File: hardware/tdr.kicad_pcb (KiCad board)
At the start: 4 copper layers, 101 x 47 mm, 240 parts, among them J201 Conn_02x01, J202 Conn_Coaxial, J203 Conn_Coaxial, J204 Conn_Coaxial, J205 Conn_Coaxial, J207 Conn_Coaxial, J208 Conn_Coaxial, J209 Conn_Coaxial, J210 Barrel_Jack_Switch, J801 Conn_02x06_Counter_Clockwise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

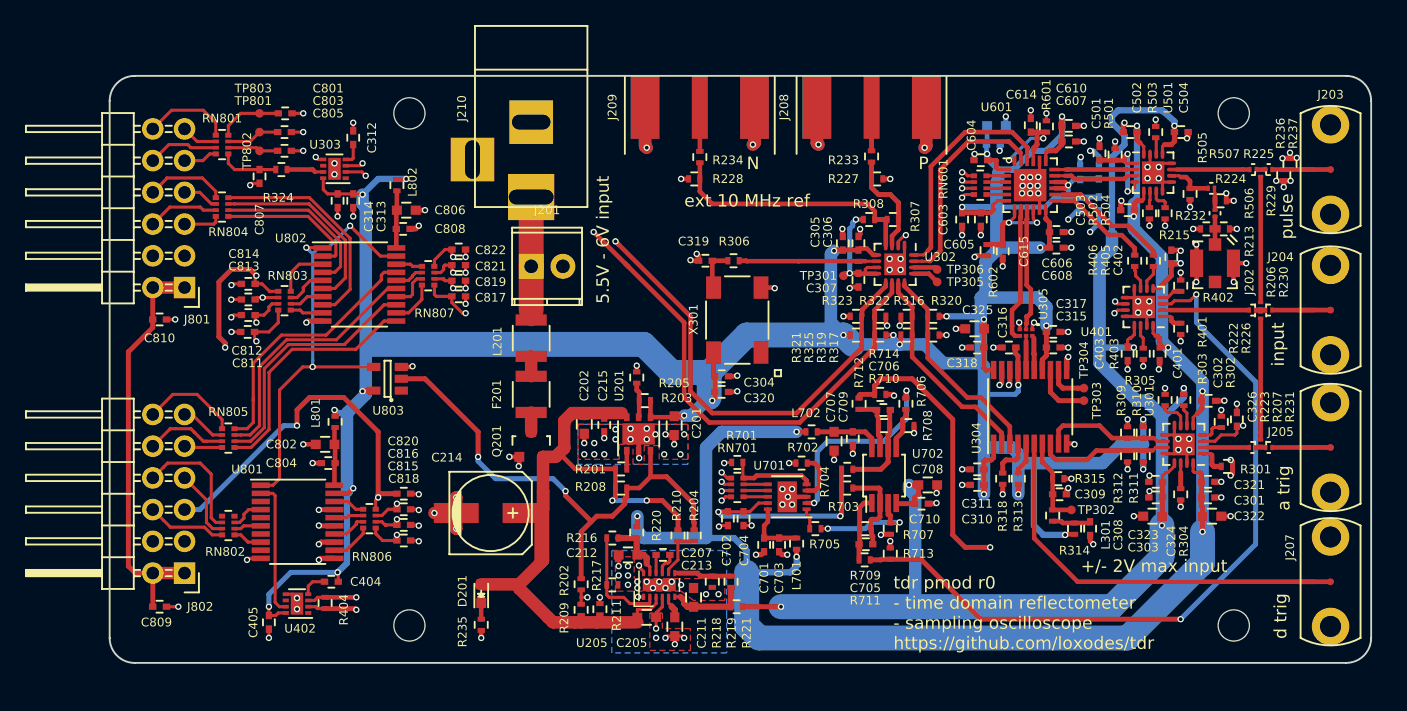
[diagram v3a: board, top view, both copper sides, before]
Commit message: cleanup of tdr layout
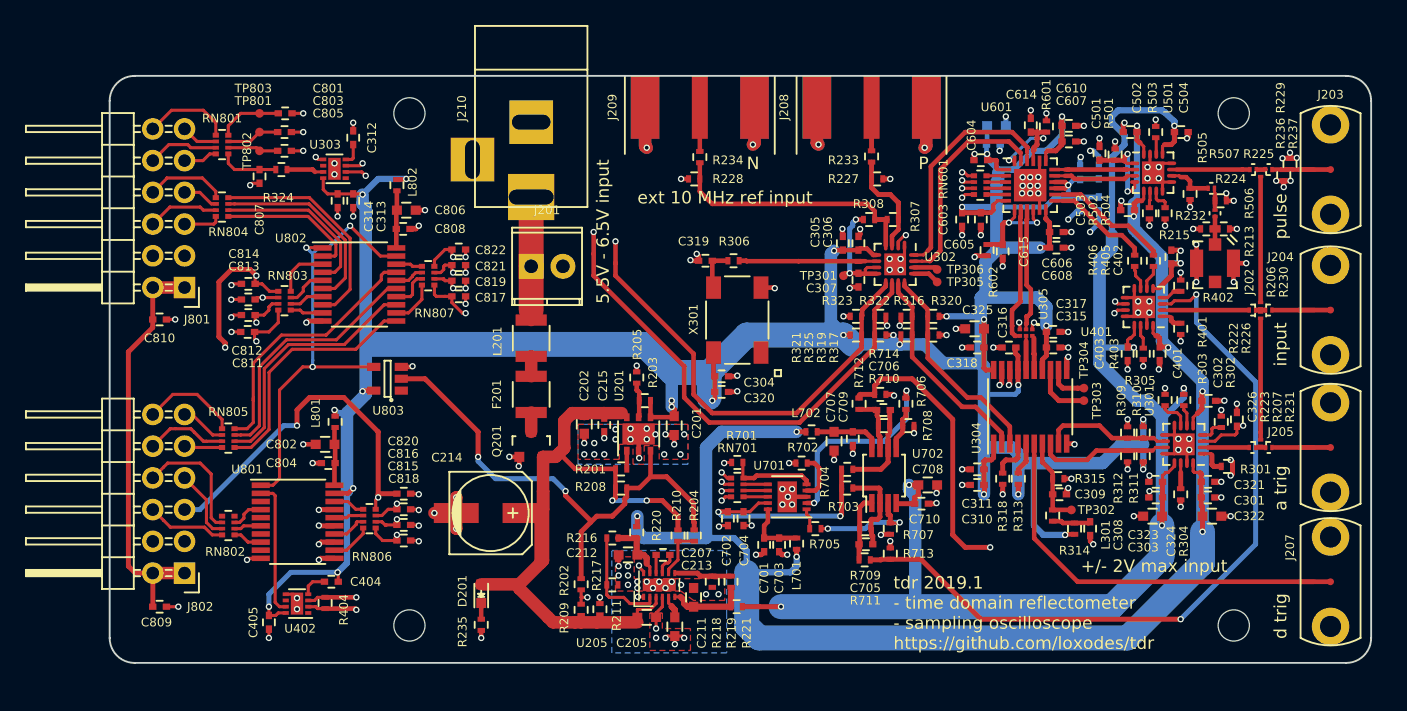
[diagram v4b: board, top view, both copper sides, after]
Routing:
- net +3V3: track 270.6 -> 271.2 mm, vias 27 -> 28
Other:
- rule pad_to_mask_clearance: 0.025 -> 0
- rule solder_mask_min_width: 0.25 -> 0.15
- board text added: "5.5V - 6.5V input"
- board text added: "ext 10 MHz ref input"
- board text added: "tdr 2019.1 - time domain reflectometer - sampling oscilloscope https://github.com/loxodes/tdr"
- board text removed: "5.5V - 6V input"
- board text removed: "ext 10 MHz ref"
- board text removed: "tdr pmod r0 - time domain reflectometer - sampling oscilloscope https://github.com/loxodes/tdr"
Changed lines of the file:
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@@
     (thickness 1.6)
     (drawings 18)
-    (tracks 2160)
+    (tracks 2161)
     (zones 0)
     (modules 240)
@@
   (layers
     (0 F.Cu signal)
-    (1 In1.Cu signal hide)
+    (1 In1.Cu signal)
     (2 In2.Cu signal)
     (31 B.Cu signal)
@@
   )
   (setup
-    (last_trace_width 0.5)
+    (last_trace_width 0.25)
     (user_trace_width 0.37)
     (user_trace_width 0.4)
@@
     (pad_size 1.524 1.524)
     (pad_drill 0.762)
-    (pad_to_mask_clearance 0.025)
-    (solder_mask_min_width 0.25)
+    (pad_to_mask_clearance 0)
+    (solder_mask_min_width 0.15)
     (aux_axis_origin 0 0)
     (visible_elements FFFDFF7F)
@@
     (tags "resistor 0402")
     (attr smd)
-    (fp_text reference R203 (at 2.55 -0.2) (layer F.SilkS)
+    (fp_text reference R203 (at 0.65 -2.25 90) (layer F.SilkS)
       (effects (font (size 0.7 0.7) (thickness 0.15)))
     )
@@
     (tags "resistor 0402")
     (attr smd)
-    (fp_text reference R205 (at 0.45 -3) (layer F.SilkS)
+    (fp_text reference R205 (at -2.65 -0.05 90) (layer F.SilkS)
       (effects (font (size 0.7 0.7) (thickness 0.15)))
     )
@@
     (tags "resistor 0201")
     (attr smd)
-    (fp_text reference R229 (at -0.2 -2.5 270) (layer F.SilkS)
+    (fp_text reference R229 (at -0.95 5.75 270) (layer F.SilkS)
       (effects (font (size 0.7 0.7) (thickness 0.15)))
     )
@@
     (effects (font (size 1 1) (thickness 0.25)) (justify left))
   )
-  (gr_text "ext 10 MHz ref" (at 135 69) (layer F.SilkS)
+  (gr_text "ext 10 MHz ref input" (at 131.25 68.75) (layer F.SilkS)
     (effects (font (size 1 1) (thickness 0.25)) (justify left))
   )
-  (gr_text "5.5V - 6V input\n" (at 128.5 77.25 90) (layer F.SilkS)
+  (gr_text "5.5V - 6.5V input\n" (at 128.5 77.25 90) (layer F.SilkS)
     (effects (font (size 1 1) (thickness 0.25)) (justify left))
   )
-  (gr_text "tdr pmod r0\n- time domain reflectometer\n- sampling oscilloscope\nhttps://github.com/loxodes/tdr" (at 151.75 102) (layer F.SilkS)
+  (gr_text "tdr 2019.1\n- time domain reflectometer\n- sampling oscilloscope\nhttps://github.com/loxodes/tdr" (at 151.75 102) (layer F.SilkS)
     (effects (font (size 1 1) (thickness 0.25)) (justify left))
   )
@@
     (effects (font (size 1 1) (thickness 0.25)))
   )
-  (gr_text "a trig" (at 183 92 90) (layer F.SilkS)
+  (gr_text "a trig" (at 182.75 92 90) (layer F.SilkS)
     (effects (font (size 1 1) (thickness 0.25)))
   )
-  (gr_text input (at 182.55 80.5 90) (layer F.SilkS)
+  (gr_text input (at 182.75 80.5 90) (layer F.SilkS)
     (effects (font (size 1 1) (thickness 0.25)))
   )
-  (gr_text pulse (at 183.25 70.25 90) (layer F.SilkS)
+  (gr_text pulse (at 182.75 70.25 90) (layer F.SilkS)
     (effects (font (size 1 1) (thickness 0.25)))
   )
@@
   (segment (start 134.122357 86.327643) (end 134.2 86.25) (width 0.37) (layer F.Cu) (net 2))
   (segment (start 132.302946 86.327643) (end 134.122357 86.327643) (width 0.37) (layer F.Cu) (net 2))
-  (via (at 135 86.2) (size 0.51) (drill 0.3) (layers F.Cu B.Cu) (net 2))
-  (segment (start 134.2 86.25) (end 134.95 86.25) (width 0.37) (layer F.Cu) (net 2))
-  (segment (start 134.95 86.25) (end 135 86.2) (width 0.37) (layer F.Cu) (net 2))
   (segment (start 160.075 66.5) (end 160 66.425) (width 0.25) (layer F.Cu) (net 2))
   (segment (start 160.75 66.5) (end 160.075 66.5) (width 0.25) (layer F.Cu) (net 2))
@@
   (segment (start 137 82.75) (end 140 79.75) (width 2) (layer B.Cu) (net 2))
   (segment (start 140 79.75) (end 147.75 79.75) (width 2) (layer B.Cu) (net 2))
-  (segment (start 135.55 86.2) (end 137 84.75) (width 1) (layer B.Cu) (net 2))
-  (segment (start 135 86.2) (end 135.55 86.2) (width 1) (layer B.Cu) (net 2))
   (segment (start 109.25 68.5) (end 109.25 69.25) (width 1) (layer B.Cu) (net 2))
   (segment (start 109.25 69.25) (end 109.5 69.5) (width 1) (layer B.Cu) (net 2))
@@
   (segment (start 165.25 63.75) (end 164 65) (width 0.5) (layer B.Cu) (net 2))
   (segment (start 165.25 62.25) (end 165.25 63.75) (width 0.5) (layer B.Cu) (net 2))
+  (via (at 134 85.5) (size 0.51) (drill 0.3) (layers F.Cu B.Cu) (net 2))
+  (segment (start 134 85.5) (end 134 82.75) (width 1) (layer B.Cu) (net 2))
+  (via (at 134 85) (size 0.51) (drill 0.3) (layers F.Cu B.Cu) (net 2))
+  (segment (start 134 85.5) (end 134 85) (width 0.4) (layer F.Cu) (net 2))
+  (segment (start 134 85.5) (end 134.2 85.7) (width 0.4) (layer F.Cu) (net 2))
+  (segment (start 134.2 86.25) (end 134.2 85.7) (width 0.4) (layer F.Cu) (net 2))
   (segment (start 123.4 94) (end 123.7 93.7) (width 1) (layer F.Cu) (net 3))
   (segment (start 122.25082 94) (end 123.4 94) (width 1) (layer F.Cu) (net 3))
@@
   (segment (start 149.2 78.25) (end 149.2 79.75) (width 0.37) (layer F.Cu) (net 58))
   (segment (start 149.2 79.75) (end 149.2 80.42) (width 0.37) (layer F.Cu) (net 58))
-  (segment (start 149.2 79.75) (end 149.2 80.8) (width 0.37) (layer F.Cu) (net 58))
-  (segment (start 144 86) (end 137.25 86) (width 0.37) (layer F.Cu) (net 58))
-  (segment (start 137.25 86) (end 135.5 84.25) (width 0.37) (layer F.Cu) (net 58))
-  (segment (start 149.2 80.8) (end 144 86) (width 0.37) (layer F.Cu) (net 58))
-  (segment (start 135.5 84.25) (end 135.5 78.25) (width 0.37) (layer F.Cu) (net 58))
-  (segment (start 135.5 78.25) (end 129.75 72.5) (width 0.37) (layer F.Cu) (net 58))
-  (segment (start 129.75 72.5) (end 129.5 72.25) (width 0.37) (layer F.Cu) (net 58))
   (via (at 129.5 72.25) (size 0.51) (drill 0.3) (layers F.Cu B.Cu) (net 58))
   (via (at 109.5 67) (size 0.51) (drill 0.3) (layers F.Cu B.Cu) (net 58))
@@
   (segment (start 118.75 72.25) (end 113 66.5) (width 0.37) (layer In2.Cu) (net 58))
   (segment (start 129.5 72.25) (end 118.75 72.25) (width 0.37) (layer In2.Cu) (net 58))
+  (segment (start 129.5 74) (end 129.5 72.25) (width 0.37) (layer F.Cu) (net 58))
+  (segment (start 129.5 75) (end 129.5 74) (width 0.37) (layer F.Cu) (net 58))
+  (segment (start 149.2 79.75) (end 149.2 80.8) (width 0.37) (layer F.Cu) (net 58))
+  (segment (start 149.2 80.8) (end 144 86) (width 0.37) (layer F.Cu) (net 58))
+  (segment (start 135.75 84.5) (end 135.75 81.25) (width 0.37) (layer F.Cu) (net 58))
+  (segment (start 144 86) (end 137.25 86) (width 0.37) (layer F.Cu) (net 58))
+  (segment (start 135.75 81.25) (end 129.5 75) (width 0.37) (layer F.Cu) (net 58))
+  (segment (start 137.25 86) (end 135.75 84.5) (width 0.37) (layer F.Cu) (net 58))
   (segment (start 106.1 66.69) (end 105.44 66.69) (width 0.25) (layer F.Cu) (net 59))
   (segment (start 105.25 66.5) (end 105.44 66.69) (width 0.37) (layer F.Cu) (net 59))
@@
   (segment (start 150.25 77.75) (end 150.25 78.25) (width 0.37) (layer F.Cu) (net 147))
   (segment (start 150.25 78.25) (end 150.25 79.75) (width 0.37) (layer F.Cu) (net 147))
-  (segment (start 150.25 79.75) (end 150.25 80.75) (width 0.37) (layer F.Cu) (net 147))
-  (segment (start 150.25 80.75) (end 144.25 86.75) (width 0.37) (layer F.Cu) (net 147))
-  (segment (start 137 86.75) (end 135 84.75) (width 0.37) (layer F.Cu) (net 147))
-  (segment (start 135 84.75) (end 135 78.75) (width 0.37) (layer F.Cu) (net 147))
-  (segment (start 144.25 86.75) (end 137 86.75) (width 0.37) (layer F.Cu) (net 147))
-  (segment (start 135 78.75) (end 130.5 74.25) (width 0.37) (layer F.Cu) (net 147))
-  (segment (start 130.5 74.25) (end 130.25 74) (width 0.37) (layer F.Cu) (net 147))
   (via (at 109.25 66) (size 0.51) (drill 0.3) (layers F.Cu B.Cu) (net 147))
   (segment (start 107.9 66.19) (end 109.06 66.19) (width 0.25) (layer F.Cu) (net 147))
@@
   (segment (start 119.5 71.5) (end 127.75 71.5) (width 0.37) (layer In2.Cu) (net 147))
   (via (at 127.75 71.5) (size 0.51) (drill 0.3) (layers F.Cu B.Cu) (net 147))
-  (segment (start 128.75 72.5) (end 127.75 71.5) (width 0.37) (layer F.Cu) (net 147))
-  (segment (start 130.5 74.25) (end 128.75 72.5) (width 0.37) (layer F.Cu) (net 147))
+  (segment (start 135 84.75) (end 135 82.25) (width 0.37) (layer F.Cu) (net 147))
+  (segment (start 150.25 80.75) (end 144.25 86.75) (width 0.37) (layer F.Cu) (net 147))
+  (segment (start 127.75 75) (end 127.75 73.25) (width 0.37) (layer F.Cu) (net 147))
+  (segment (start 150.25 79.75) (end 150.25 80.75) (width 0.37) (layer F.Cu) (net 147))
+  (segment (start 135 82.25) (end 127.75 75) (width 0.37) (layer F.Cu) (net 147))
+  (segment (start 144.25 86.75) (end 137 86.75) (width 0.37) (layer F.Cu) (net 147))
+  (segment (start 127.75 73.25) (end 127.75 71.5) (width 0.37) (layer F.Cu) (net 147))
+  (segment (start 137 86.75) (end 135 84.75) (width 0.37) (layer F.Cu) (net 147))
   (segment (start 172.565516 74.879082) (end 172.565516 74.254082) (width 0.25) (layer F.Cu) (net 148))
   (segment (start 172.040516 76.029082) (end 172.040516 75.404082) (width 0.25) (layer F.Cu) (net 148))

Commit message: fixed CML termination.. ready to order?
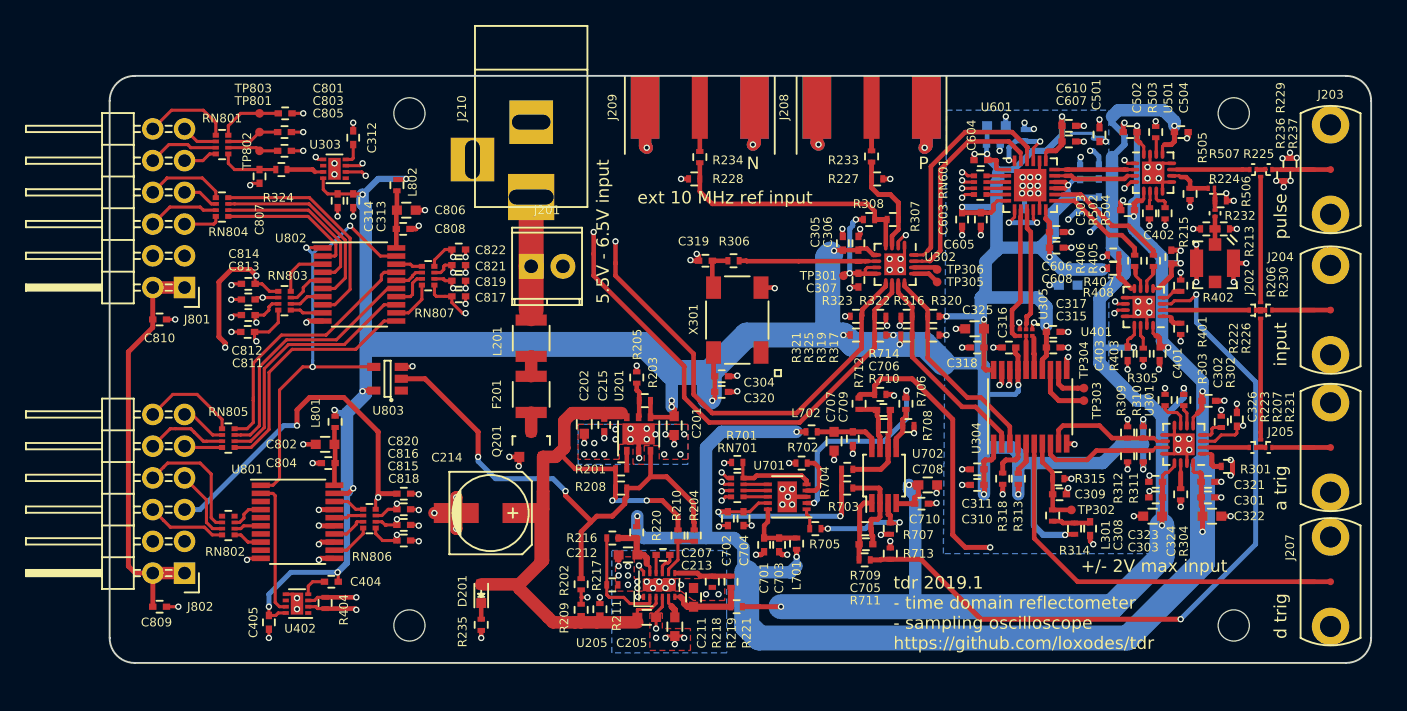
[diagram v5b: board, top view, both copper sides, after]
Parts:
- removed C614, C615: 10 nF, Capacitors_SMD:C_0402
- removed R501: 50, Resistors_SMD:R_0402
- added C406: 2.2 uF, Capacitors_SMD:C_0603, B.Cu at (165.8, 75.8)
- added R407: JMP, Resistors_SMD:R_0402, F.Cu at (169.3, 73.3)
- added R408: JMP, Resistors_SMD:R_0402, F.Cu at (169.3, 74.4)
- C308, C309, C401, C402, C403, C501, C502, C503, C504: value .01 uF -> 10 nF
- R309, R311: value 125 -> 50
- R310, R312: value 84 -> DNP
- R601, R602: moved to B.Cu
- moved R602 4.04 mm to (162.2, 70.2), turned to 270 degrees
- moved R601 1.88 mm to (162.2, 63.8)
- moved C501 1.50 mm to (168.2, 63.7)
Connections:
- C501 pad 1: Net-(C501-Pad1) -> +3V3
- U401 pad 8: GND -> Net-(R407-Pad1)
- U501 pad 1: Net-(C501-Pad1) -> +3V3
- U501 pad 4: Net-(C501-Pad1) -> +3V3
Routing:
- net +3V3: track 271.2 -> 304.2 mm, vias 28 -> 32
- net Net-(C501-Pad1): track 7.80 -> 0.00 mm, vias 2 -> 0
- net -5VA: track 111.8 -> 116.2 mm
- net Net-(R407-Pad1): track 0.00 -> 3.38 mm
- net Net-(R602-Pad2): track 8.03 -> 4.66 mm
- net Net-(R601-Pad2): track 8.12 -> 6.10 mm
- net GND: track 166.7 -> 167.3 mm, vias 222 -> 221
- added copper zone on B.Cu, net +3V3
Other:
- rule pad_to_mask_clearance: 0 -> 0.01
